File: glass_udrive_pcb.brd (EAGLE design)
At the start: 8.5 x 19 mm, 14 parts, among them IC1 OPA129U, J1 OMNETICS_A75243-001

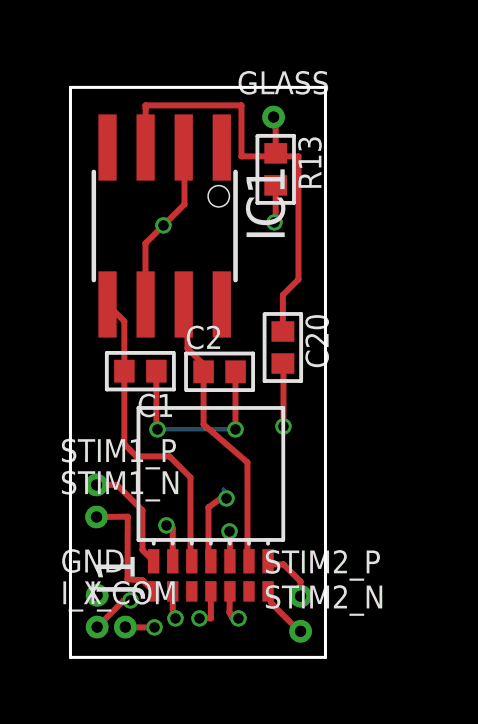
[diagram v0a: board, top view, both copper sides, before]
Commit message: smashed labels
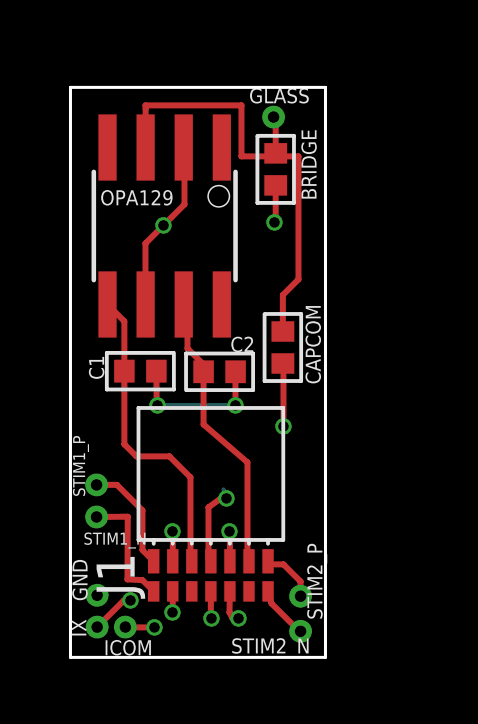
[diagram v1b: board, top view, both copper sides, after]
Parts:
- renumbered C20 to CAPCOM, IC1 to OPA129, I_COM to ICOM, I_X to IX, R13 to BRIDGE
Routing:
- net GND: track 9.32 -> 7.72 mm
